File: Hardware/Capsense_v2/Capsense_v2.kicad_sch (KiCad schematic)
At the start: 7 parts, among them U1 MSP430FR2676TRHBR, Y1 32k768

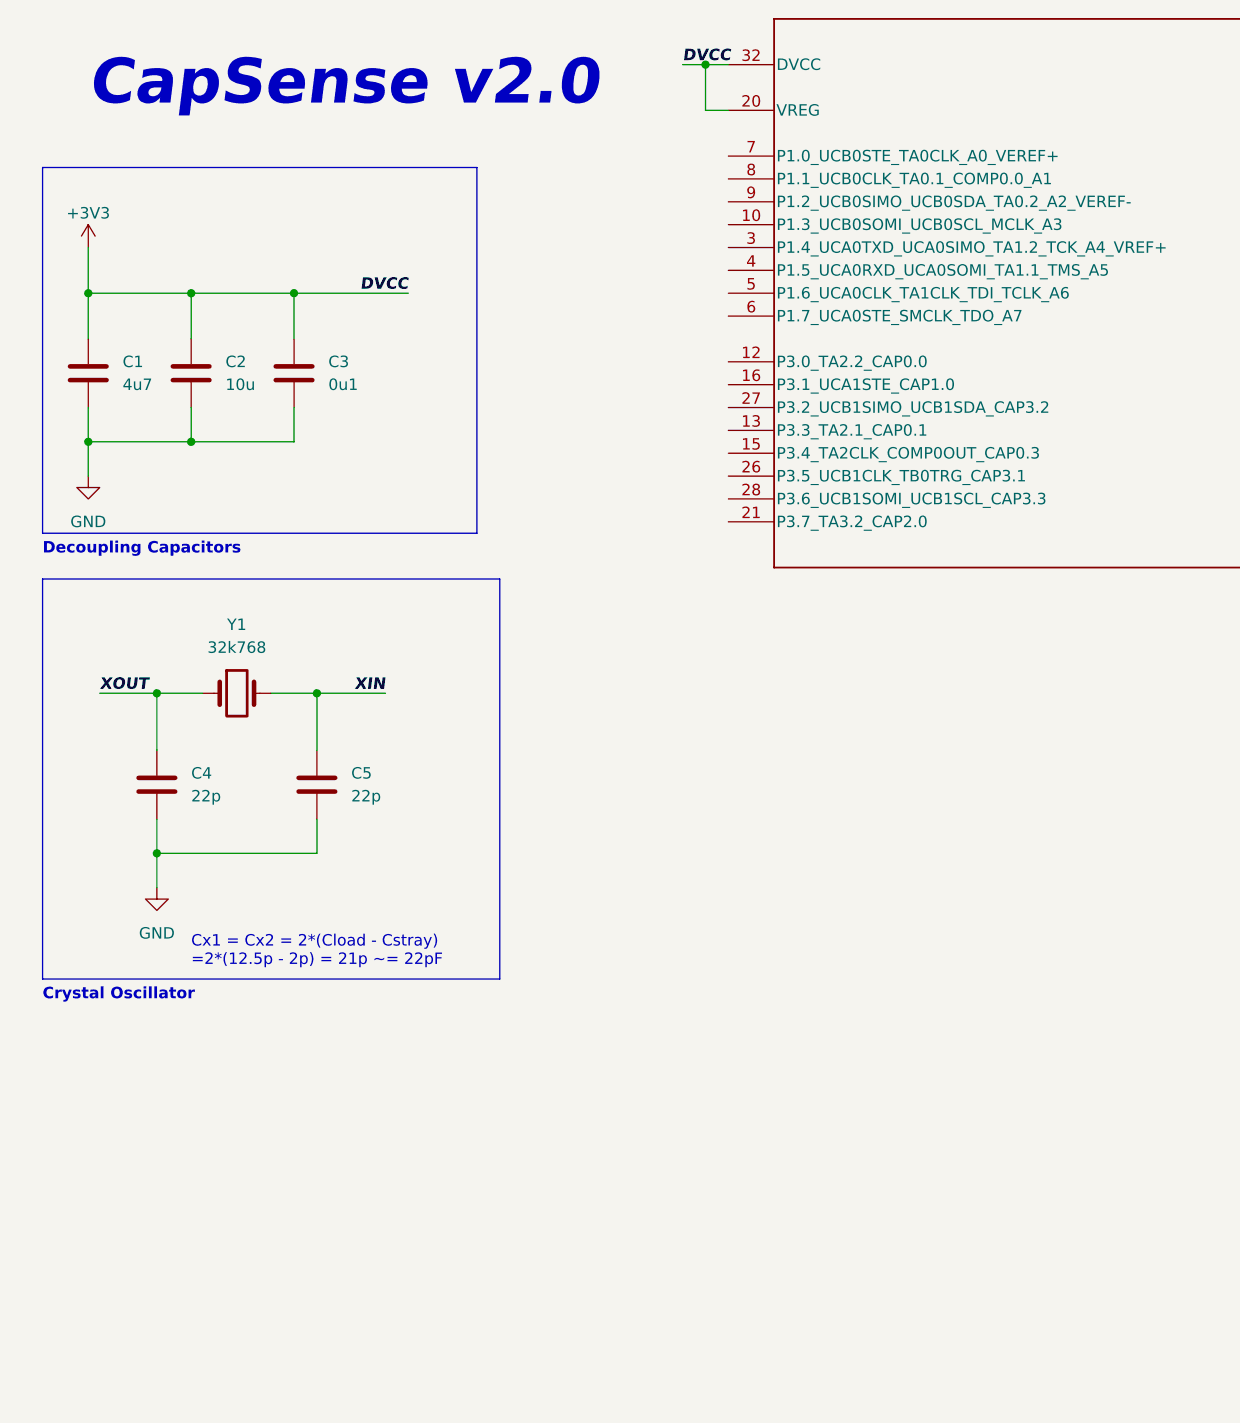
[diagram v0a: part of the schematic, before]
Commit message: Added I2C and JTAG in Schematic
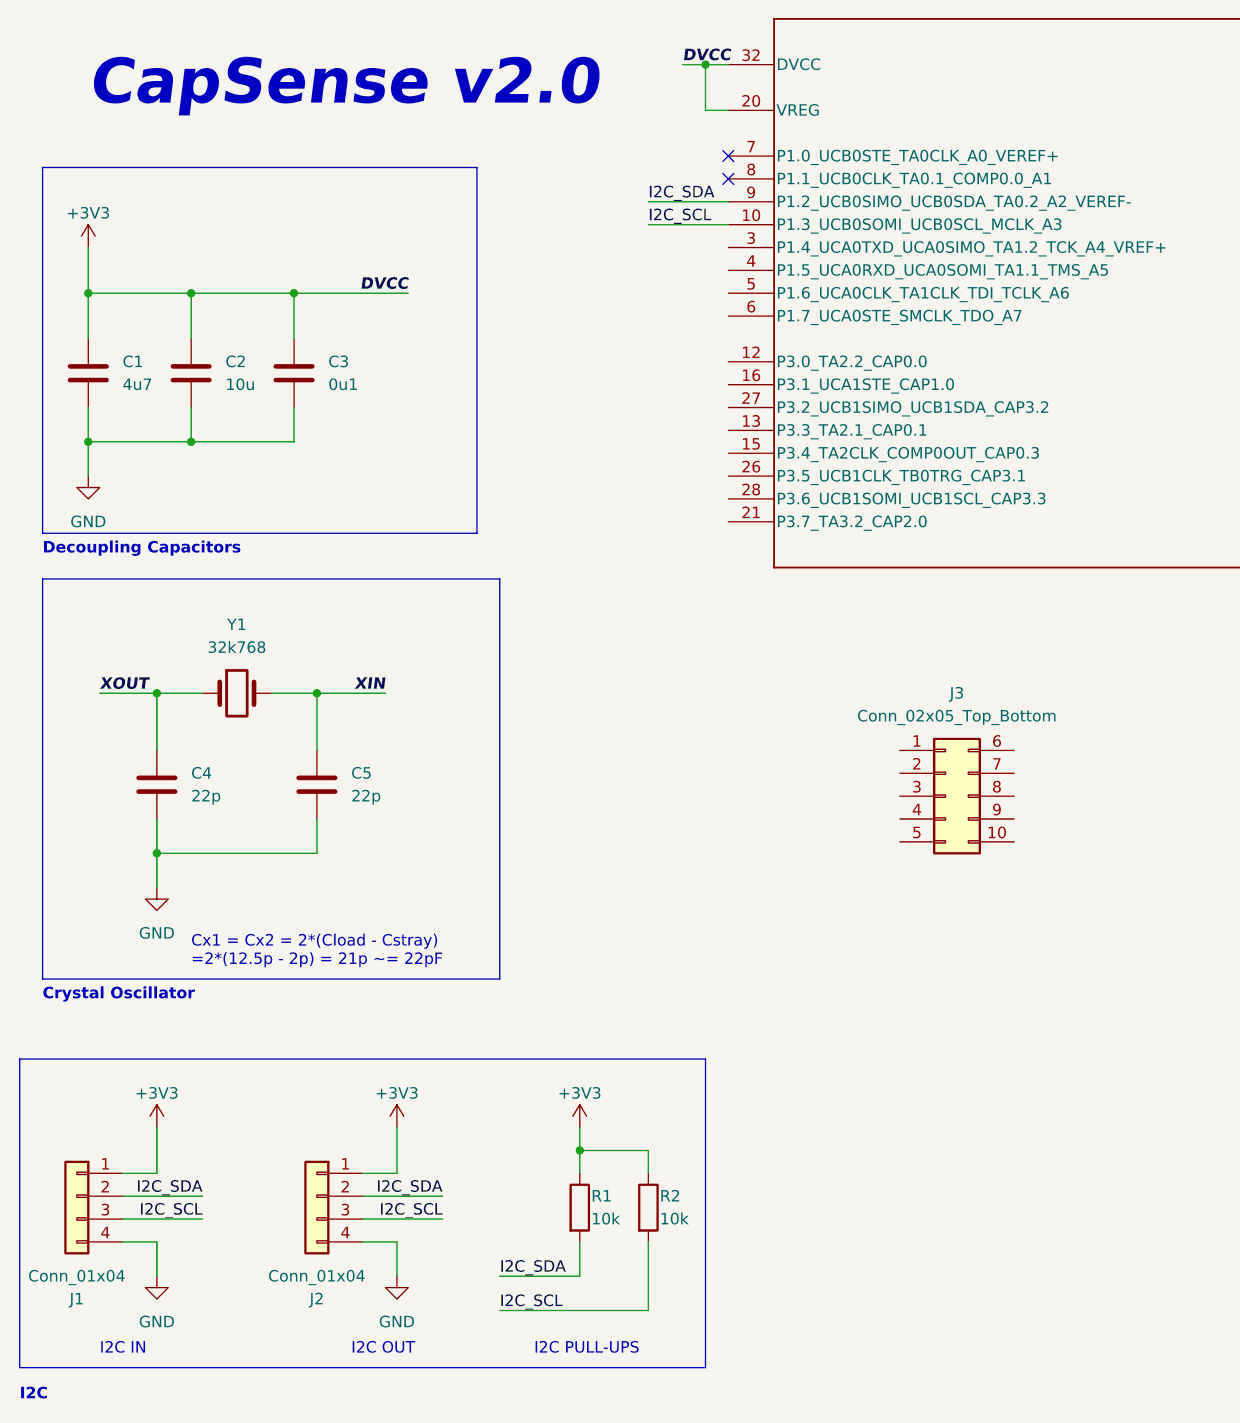
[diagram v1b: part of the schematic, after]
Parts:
- added J1, J2: Conn_01x04, symbol Connector_Generic:Conn_01x04
- added J3: Conn_02x05_Top_Bottom, symbol Connector_Generic:Conn_02x05_Top_Bottom
- added R1, R2: 10k, symbol Device:R
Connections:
- net +3V3: now also J1.1 (Pin_1), J2.1 (Pin_1), R1.1, R2.1
- net GND: now also J1.4 (Pin_4), J2.4 (Pin_4)
- net I2C_SCL: now reaches U1.10 (P1.3_UCB0SOMI_UCB0SCL_MCLK_A3)
- net I2C_SCL: now also J1.3 (Pin_3), J2.3 (Pin_3), R2.2
- net I2C_SDA: now reaches U1.9 (P1.2_UCB0SIMO_UCB0SDA_TA0.2_A2_VEREF-)
- net I2C_SDA: now also J1.2 (Pin_2), J2.2 (Pin_2), R1.2
- no-connect marks 0 -> 2
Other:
- note added: "I2C"
- note added: "I2C IN"
- note added: "I2C OUT"
- note added: "I2C PULL-UPS"

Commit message: Completed Schematic for Version 2
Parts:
- removed J3: Conn_02x05_Top_Bottom, symbol Connector_Generic:Conn_02x05_Top_Bottom
- added C6: 1n, symbol Device:C
- added C7: 10n, symbol Device:C
- added D1: GREEN, symbol Device:LED
- added D2: RED, symbol Device:LED
- added D3: BLUE, symbol Device:LED
- added J3: Conn_02x07_Odd_Even, symbol Connector_Generic:Conn_02x07_Odd_Even
- added J4: Conn_01x03, symbol Connector_Generic:Conn_01x03
- added J5: DINA, symbol Connector_Generic:Conn_01x16
- added J6: DINB, symbol Connector_Generic:Conn_01x16
- added J7: DINC, symbol Connector_Generic:Conn_01x16
- added J8: Conn_01x02, symbol Connector_Generic:Conn_01x02
- added R10, R11, R12, R13, R14, R15, R16, R17, R18, R19, R20, R21, R22, R23, R8, R9: 470, symbol Device:R
- added R3: 47k, symbol Device:R
- added R4, R5, R6, R7: 10k, symbol Device:R
- added SW1: SW_Push, symbol Switch:SW_Push
- added SW2: SW_SPDT, symbol Switch:SW_SPDT
- added U2: TPS73633DBV, Package_TO_SOT_SMD:SOT-23-5, symbol Regulator_Linear:TPS73633DBV
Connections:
- net +3V3: now also D1.1 (K), D1.2 (A), J4.2 (Pin_2), R3.1, R4.1, SW2.3 (C), U2.5 (OUT)
- net GND: now also C6.2, C7.2, J3.9 (Pin_9), J6.1 (Pin_1), J6.10 (Pin_10), J6.11 (Pin_11), J6.12 (Pin_12), J6.13 (Pin_13), J6.14 (Pin_14), J6.15 (Pin_15), J6.16 (Pin_16), J6.2 (Pin_2), J6.3 (Pin_3), J6.4 (Pin_4), J6.5 (Pin_5), J6.6 (Pin_6), J6.7 (Pin_7), J6.8 (Pin_8), J6.9 (Pin_9), J7.1 (Pin_1), J7.10 (Pin_10), J7.11 (Pin_11), J7.12 (Pin_12), J7.13 (Pin_13), J7.14 (Pin_14), J7.15 (Pin_15), J7.16 (Pin_16), J7.2 (Pin_2), J7.3 (Pin_3), J7.4 (Pin_4), J7.5 (Pin_5), J7.6 (Pin_6), J7.7 (Pin_7), J7.8 (Pin_8), J7.9 (Pin_9), J8.1 (Pin_1), R4.2, R5.2, R6.2, SW1.1, SW2.1 (A), U2.2 (GND)
- net RST: now reaches U1.1 (RST_NMI_SBWTDIO_N)
- net RST: now also C6.1, J3.11 (Pin_11), R3.2, SW1.2
- net P2.2_MODE: now reaches U1.11 (P2.2_SYNC_ACLK_COMP0.1)
- net P2.2_MODE: now also R7.2
- net CAP0.0: now reaches U1.12 (P3.0_TA2.2_CAP0.0)
- net CAP0.0: now also R8.1
- net CAP0.1: now reaches U1.13 (P3.3_TA2.1_CAP0.1)
- net CAP0.1: now also R9.1
- net CAP0.2: now reaches U1.14 (P2.3_TA2.0_CAP0.2)
- net CAP0.2: now also R10.1
- net CAP0.3: now reaches U1.15 (P3.4_TA2CLK_COMP0OUT_CAP0.3)
- net CAP0.3: now also R11.1
- net CAP1.0: now reaches U1.16 (P3.1_UCA1STE_CAP1.0)
- net CAP1.0: now also R12.1
- net CAP1.1: now reaches U1.17 (P2.4_UCA1CLK_CAP1.1)
- net CAP1.1: now also R13.1
- net CAP1.2: now reaches U1.18 (P2.5_UCA1RXD_UCA1SOMI_CAP1.2)
- net CAP1.2: now also R14.1
- net CAP1.3: now reaches U1.19 (P2.6_UCA1TXD_UCA1SIMO_CAP1.3)
- net CAP1.3: now also R15.1
- net TEST: now reaches U1.2 (TEST_SBWTCK)
- net TEST: now also J3.8 (Pin_8)
- net CAP2.0: now reaches U1.21 (P3.7_TA3.2_CAP2.0)
- net CAP2.0: now also R16.1
- net CAP2.1: now reaches U1.22 (P4.0_TA3.1_CAP2.1)
- net CAP2.1: now also R17.1
- net CAP2.2: now reaches U1.23 (P4.1_TA3.0_CAP2.2)
- net CAP2.2: now also R18.1
- net CAP2.3: now reaches U1.24 (P4.2_TA3CLK_CAP2.3)
- net CAP2.3: now also R20.1
- net CAP3.0: now reaches U1.25 (P2.7_UCB1STE_CAP3.0)
- net CAP3.0: now also R19.1
- net CAP3.1: now reaches U1.26 (P3.5_UCB1CLK_TB0TRG_CAP3.1)
- net CAP3.1: now also R21.1
- net CAP3.2: now reaches U1.27 (P3.2_UCB1SIMO_UCB1SDA_CAP3.2)
- net CAP3.2: now also R22.1
- net CAP3.3: now reaches U1.28 (P3.6_UCB1SOMI_UCB1SCL_CAP3.3)
- net CAP3.3: now also R23.1
- net TCK: now reaches U1.3 (P1.4_UCA0TXD_UCA0SIMO_TA1.2_TCK_A4_VREF+)
- net TCK: now also J3.7 (Pin_7)
- net TMS: now reaches U1.4 (P1.5_UCA0RXD_UCA0SOMI_TA1.1_TMS_A5)
- net TMS: now also J3.5 (Pin_5)
- net TDI: now reaches U1.5 (P1.6_UCA0CLK_TA1CLK_TDI_TCLK_A6)
- net TDI: now also J3.3 (Pin_3)
- net TDO: now reaches U1.6 (P1.7_UCA0STE_SMCLK_TDO_A7)
- net TDO: now also J3.1 (Pin_1)
- net P1.0_LED: now reaches U1.7 (P1.0_UCB0STE_TA0CLK_A0_VEREF+)
- net P1.0_LED: now also D2.1 (K), D2.2 (A), R5.1
- net P1.1_LED: now reaches U1.8 (P1.1_UCB0CLK_TA0.1_COMP0.0_A1)
- net P1.1_LED: now also D3.1 (K), D3.2 (A), R6.1
- new net: J5.3 (Pin_3), R21.2
- new net: R7.1, SW2.2 (B)
- new net: J5.14 (Pin_14), R10.2
- new net: J5.5 (Pin_5), R20.2
- new net: J5.9 (Pin_9), R15.2
- new net: J5.8 (Pin_8), R16.2
- new net: J5.2 (Pin_2), R22.2
- new net: J5.15 (Pin_15), R9.2
- new net: J5.1 (Pin_1), R23.2
- new net: J8.2 (Pin_2), U2.1 (IN), U2.3 (EN)
- new net: J5.7 (Pin_7), R17.2
- new net: C7.1, U2.4 (NR)
- new net: J5.12 (Pin_12), R12.2
- new net: J5.4 (Pin_4), R19.2
- new net: J5.11 (Pin_11), R13.2
- new net: J5.13 (Pin_13), R11.2
- new net: J5.10 (Pin_10), R14.2
- new net: J5.6 (Pin_6), R18.2
- new net: J5.16 (Pin_16), R8.2
- new net VCC_MSP: J3.4 (Pin_4)
- new net VCC_TARGET: J4.1 (Pin_1)
- new net VCC_TOOL: J3.2 (Pin_2), J4.3 (Pin_3)
- no-connect marks 2 -> 5
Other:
- note added: "10nF cap is for noise reduction"
- note added: "COMM"
- note added: "CSA Connector"
- note added: "DK: 1195-1890-ND"
- note added: "HIGH = Controller LOW = Peripheral"
- note added: "If Battery/Source, jumper DVCC + Target If PGMR Adapter, jumper DVCC + Tool"
- note added: "Input Power and LDO Regulator"
- note added: "JTAG Programming"
- note added: "Mode Switch"
- note added: "PWR"
- note added: "Reset"
- note added: "SEN"
- note added: "Status LEDs"
- company: (none) -> AESIR Lab
- title: (none) -> CapSense
- moved on the sheet: J1, J2, R1, R2

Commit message: Completed PCB Layout
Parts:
- added H1, H2, H3, H4: MountingHole, MountingHole:MountingHole_2.2mm_M2, symbol Mechanical:MountingHole
- C1, C2, C4, C5, C6, C7: footprint (none) -> Capacitor_SMD:C_0805_2012Metric
- C3: footprint (none) -> Capacitor_SMD:C_0603_1608Metric
- D1, D2, D3: footprint (none) -> LED_SMD:LED_0805_2012Metric
- J1: footprint (none) -> Connector_PinSocket_2.54mm:PinSocket_1x04_P2.54mm_Horizontal
- J2: footprint (none) -> Connector_PinHeader_2.54mm:PinHeader_1x04_P2.54mm_Horizontal
- J3: footprint (none) -> Connector_IDC:IDC-Header_2x07_P2.54mm_Vertical
- J4: footprint (none) -> Connector_PinHeader_2.54mm:PinHeader_1x03_P2.54mm_Vertical
- J5: footprint (none) -> AESIRLab:CSA_48PN_RECPT
- J6, J7: footprint (none) -> Connector_PinSocket_2.54mm:PinSocket_1x16_P2.54mm_Vertical
- J8: footprint (none) -> Connector_JST:JST_PH_S2B-PH-K_1x02_P2.00mm_Horizontal
- R1, R10, R11, R12, R13, R14, R15, R16, R17, R18, R19, R2, R20, R21, R22, R23, R3, R4, R5, R6, R7, R8, R9: footprint (none) -> Resistor_SMD:R_0805_2012Metric
- SW1: footprint (none) -> Button_Switch_THT:SW_Tactile_SPST_Angled_PTS645Vx39-2LFS
- SW2: footprint (none) -> Button_Switch_SMD:SW_SPDT_PCM12
- U1: footprint RHB0032E -> MSP430FR2676:RHB0032E
- Y1: footprint (none) -> Crystal:Crystal_SMD_3215-2Pin_3.2x1.5mm
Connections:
- net VCC_MSP is gone; now on net VCC_TARGET: J3.4 (Pin_4)
- net +3V3: no longer C3.1, D1.1 (K), R4.1, U1.20 (VREG)
- net CAP2.3: now also R19.1; no longer R20.1
- net CAP3.0: now also R20.1; no longer R19.1
- net GND: now also J8.2 (Pin_2); no longer J8.1 (Pin_1)
- net P1.0_LED: no longer D2.1 (K), R5.1
- net P1.1_LED: no longer D3.1 (K), R6.1
- net at R20.2: now also J5.4 (Pin_4); no longer J5.5 (Pin_5)
- net at U2.1 (IN), U2.3 (EN): now also J8.1 (Pin_1); no longer J8.2 (Pin_2)
- net at R19.2: now also J5.5 (Pin_5); no longer J5.4 (Pin_4)
- new net: D3.1 (K), R6.1
- new net: D2.1 (K), R5.1
- new net: D1.1 (K), R4.1
- new net VREG: C3.1, U1.20 (VREG)
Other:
- moved on the sheet: J8, R19, R20
